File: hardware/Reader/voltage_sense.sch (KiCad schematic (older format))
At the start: 5 parts

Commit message: Fixed bugs on the reader schematic. Exported Schematic Electrical report
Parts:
- C_VS_1: Manufacturer (none) -> Yageo; Part Name (none) -> CC0603JRX7R8BB104; Vendor (none) -> DigiKey Canada; digikeypn (none) -> 311-1777-1-ND
- D_VS_1, D_VS_2: Manufacturer (none) -> STMicroelectronics; Part Name (none) -> BAT46; Vendor (none) -> DigiKey Canada; digikeypn (none) -> 497-3768-1-ND
- R_VS_1: Manufacturer (none) -> Panasonic Electronic Components; Vendor (none) -> DigiKey Canada; digikeypn (none) -> P123106CT-ND
- R_VS_2: Manufacturer (none) -> Panasonic Electronic Components; Vendor (none) -> DigiKey Canada; digikeypn (none) -> P122414CT-ND
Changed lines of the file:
@@
 $Descr USLetter 11000 8500
 encoding utf-8
-Sheet 16 19
+Sheet 17 19
 Title "CANnect Reader | Voltage Sense"
 Date "2020-10-25"
@@
 Comment4 "Component Identifier: VS"
 $EndDescr
+Wire Notes Line
+	1750 1350 1750 4150
+Wire Notes Line
+	1750 4150 4650 4150
+Wire Notes Line
+	4650 4150 4650 1350
+Wire Notes Line
+	4650 1350 1750 1350
+Text Notes 2050 1500 2    50   ~ 0
+Typical
+Wire Wire Line
+	2850 2050 2850 1750
 $Comp
-L Device:R_Small R_VS_2
-U 1 1 5FD5DF8C
-P 2850 2800
-F 0 "R_VS_2" H 2909 2846 50  0000 L CNN
-F 1 "10k 1%" H 2909 2755 50  0000 L CNN
-F 2 "footprints:RESC3216X70N" H 2850 2800 50  0001 C CNN
-F 3 "https://industrial.panasonic.com/cdbs/www-data/pdf/RDA0000/AOA0000C304.pdf" H 2850 2800 50  0001 C CNN
-F 4 "ERJ-1GNF1002C" H 2850 2800 50  0001 C CNN "Part Name"
-	1    2850 2800
+L Device:R_Small R_VS_1
+U 1 1 6007733F
+P 2850 2150
+F 0 "R_VS_1" H 2909 2196 50  0000 L CNN
+F 1 "62k 1%" H 2909 2105 50  0000 L CNN
+F 2 "footprints:RESC3216X70N" H 2850 2150 50  0001 C CNN
+F 3 "https://industrial.panasonic.com/cdbs/www-data/pdf/RDA0000/AOA0000C304.pdf" H 2850 2150 50  0001 C CNN
+F 4 "ERJ-1GNF6202C" H 2850 2150 50  0001 C CNN "Part Name"
+F 5 "Panasonic Electronic Components" H 2850 2150 50  0001 C CNN "Manufacturer"
+F 6 "DigiKey Canada" H 2850 2150 50  0001 C CNN "Vendor"
+F 7 "P123106CT-ND" H 2850 2150 50  0001 C CNN "digikeypn"
+	1    2850 2150
+	1    0    0    -1
+$EndComp
+Wire Wire Line
+	3400 2000 3400 1750
+$Comp
+L power:+3.3V #PWR0123
+U 1 1 5FD61353
+P 3400 1750
+F 0 "#PWR0123" H 3400 1600 50  0001 C CNN
+F 1 "+3.3V" H 3415 1923 50  0000 C CNN
+F 2 "" H 3400 1750 50  0001 C CNN
+F 3 "" H 3400 1750 50  0001 C CNN
+	1    3400 1750
+	1    0    0    -1
+$EndComp
+Wire Wire Line
+	3400 3650 3400 3000
+$Comp
+L power:GND #PWR0122
+U 1 1 5FD60B0C
+P 3400 3650
+F 0 "#PWR0122" H 3400 3400 50  0001 C CNN
+F 1 "GND" H 3405 3477 50  0000 C CNN
+F 2 "" H 3400 3650 50  0001 C CNN
+F 3 "" H 3400 3650 50  0001 C CNN
+	1    3400 3650
+	1    0    0    -1
+$EndComp
+Wire Wire Line
+	3400 2500 3400 2700
+Wire Wire Line
+	3400 2500 3950 2500
+Wire Wire Line
+	2850 2500 3400 2500
+Connection ~ 3400 2500
+Wire Wire Line
+	3400 2500 3400 2300
+$Comp
+L Diode:BAT46 D_VS_1
+U 1 1 5FD600B9
+P 3400 2150
+F 0 "D_VS_1" V 3354 2230 50  0000 L CNN
+F 1 "BAT46" V 3445 2230 50  0000 L CNN
+F 2 "Diode_THT:D_DO-35_SOD27_P7.62mm_Horizontal" H 3400 1975 50  0001 C CNN
+F 3 "http://www.vishay.com/docs/85662/bat46.pdf" H 3400 2150 50  0001 C CNN
+F 4 "BAT46" H 3400 2150 50  0001 C CNN "Part Name"
+F 5 "STMicroelectronics" H 3400 2150 50  0001 C CNN "Manufacturer"
+F 6 "DigiKey Canada" H 3400 2150 50  0001 C CNN "Vendor"
+F 7 "497-3768-1-ND" H 3400 2150 50  0001 C CNN "digikeypn"
+	1    3400 2150
+	0    1    1    0
+$EndComp
+$Comp
+L Diode:BAT46 D_VS_2
+U 1 1 5FD5FBA4
+P 3400 2850
+F 0 "D_VS_2" V 3354 2930 50  0000 L CNN
+F 1 "BAT46" V 3445 2930 50  0000 L CNN
+F 2 "Diode_THT:D_DO-35_SOD27_P7.62mm_Horizontal" H 3400 2675 50  0001 C CNN
+F 3 "http://www.vishay.com/docs/85662/bat46.pdf" H 3400 2850 50  0001 C CNN
+F 4 "BAT46" H 3400 2850 50  0001 C CNN "Part Name"
+F 5 "STMicroelectronics" H 3400 2850 50  0001 C CNN "Manufacturer"
+F 6 "DigiKey Canada" H 3400 2850 50  0001 C CNN "Vendor"
+F 7 "497-3768-1-ND" H 3400 2850 50  0001 C CNN "digikeypn"
+	1    3400 2850
+	0    1    1    0
+$EndComp
+Text HLabel 3950 2500 2    50   Output ~ 0
+Analog_Voltage
+$Comp
+L power:GND #PWR0112
+U 1 1 5FD5EC70
+P 2850 3650
+F 0 "#PWR0112" H 2850 3400 50  0001 C CNN
+F 1 "GND" H 2855 3477 50  0000 C CNN
+F 2 "" H 2850 3650 50  0001 C CNN
+F 3 "" H 2850 3650 50  0001 C CNN
+	1    2850 3650
+	1    0    0    -1
+$EndComp
+Wire Wire Line
+	2850 3300 2850 3650
+Wire Wire Line
+	2850 3300 2850 2900
+Connection ~ 2850 3300
+Wire Wire Line
+	2250 3300 2850 3300
+Wire Wire Line
+	2250 2950 2250 3300
+Wire Wire Line
+	2850 2500 2850 2250
+Wire Wire Line
+	2850 2500 2850 2700
+Connection ~ 2850 2500
+Wire Wire Line
+	2250 2500 2850 2500
+Wire Wire Line
+	2250 2650 2250 2500
+$Comp
+L Device:C C_VS_1
+U 1 1 5FD5E63B
+P 2250 2800
+F 0 "C_VS_1" H 2365 2846 50  0000 L CNN
+F 1 "0.1uF" H 2365 2755 50  0000 L CNN
+F 2 "footprints:CAPC1608X90" H 2288 2650 50  0001 C CNN
+F 3 "https://www.yageo.com/upload/media/product/productsearch/datasheet/mlcc/UPY-GPHC_X7R_6.3V-to-50V_18.pdf" H 2250 2800 50  0001 C CNN
+F 4 "CC0603JRX7R8BB104" H 2250 2800 50  0001 C CNN "Part Name"
+F 5 "Yageo" H 2250 2800 50  0001 C CNN "Manufacturer"
+F 6 "DigiKey Canada" H 2250 2800 50  0001 C CNN "Vendor"
+F 7 "311-1777-1-ND" H 2250 2800 50  0001 C CNN "digikeypn"
+	1    2250 2800
 	1    0    0    -1
 $EndComp
@@
 $EndComp
 $Comp
-L Device:C C_VS_1
-U 1 1 5FD5E63B
-P 2250 2800
-F 0 "C_VS_1" H 2365 2846 50  0000 L CNN
-F 1 "0.1uF" H 2365 2755 50  0000 L CNN
-F 2 "footprints:CAPC1608X90" H 2288 2650 50  0001 C CNN
-F 3 "https://www.yageo.com/upload/media/product/productsearch/datasheet/mlcc/UPY-GPHC_X7R_6.3V-to-50V_18.pdf" H 2250 2800 50  0001 C CNN
-	1    2250 2800
+L Device:R_Small R_VS_2
+U 1 1 5FD5DF8C
+P 2850 2800
+F 0 "R_VS_2" H 2909 2846 50  0000 L CNN
+F 1 "10k 1%" H 2909 2755 50  0000 L CNN
+F 2 "footprints:RESC3216X70N" H 2850 2800 50  0001 C CNN
+F 3 "https://industrial.panasonic.com/cdbs/www-data/pdf/RDA0000/AOA0000C304.pdf" H 2850 2800 50  0001 C CNN
+F 4 "ERJ-1GNF1002C" H 2850 2800 50  0001 C CNN "Part Name"
+F 5 "Panasonic Electronic Components" H 2850 2800 50  0001 C CNN "Manufacturer"
+F 6 "DigiKey Canada" H 2850 2800 50  0001 C CNN "Vendor"
+F 7 "P122414CT-ND" H 2850 2800 50  0001 C CNN "digikeypn"
+	1    2850 2800
 	1    0    0    -1
 $EndComp
-Wire Wire Line
-	2250 2650 2250 2500
-Wire Wire Line
-	2250 2500 2850 2500
-Connection ~ 2850 2500
-Wire Wire Line
-	2850 2500 2850 2700
-Wire Wire Line
-	2250 2950 2250 3300
-Wire Wire Line
-	2250 3300 2850 3300
-Wire Wire Line
-	2850 3300 2850 2900
-$Comp
-L power:GND #PWR0112
-U 1 1 5FD5EC70
-P 2850 3650
-F 0 "#PWR0112" H 2850 3400 50  0001 C CNN
-F 1 "GND" H 2855 3477 50  0000 C CNN
-F 2 "" H 2850 3650 50  0001 C CNN
-F 3 "" H 2850 3650 50  0001 C CNN
-	1    2850 3650
-	1    0    0    -1
-$EndComp
-Wire Wire Line
-	2850 3300 2850 3650
-Connection ~ 2850 3300
-Text HLabel 3950 2500 2    50   Output ~ 0
-Analog_Voltage
-$Comp
-L Diode:BAT46 D_VS_2
-U 1 1 5FD5FBA4
-P 3400 2850
-F 0 "D_VS_2" V 3354 2930 50  0000 L CNN
-F 1 "BAT46" V 3445 2930 50  0000 L CNN
-F 2 "Diode_THT:D_DO-35_SOD27_P7.62mm_Horizontal" H 3400 2675 50  0001 C CNN
-F 3 "http://www.vishay.com/docs/85662/bat46.pdf" H 3400 2850 50  0001 C CNN
-	1    3400 2850
-	0    1    1    0
-$EndComp
-$Comp
-L Diode:BAT46 D_VS_1
-U 1 1 5FD600B9
-P 3400 2150
-F 0 "D_VS_1" V 3354 2230 50  0000 L CNN
-F 1 "BAT46" V 3445 2230 50  0000 L CNN
-F 2 "Diode_THT:D_DO-35_SOD27_P7.62mm_Horizontal" H 3400 1975 50  0001 C CNN
-F 3 "http://www.vishay.com/docs/85662/bat46.pdf" H 3400 2150 50  0001 C CNN
-	1    3400 2150
-	0    1    1    0
-$EndComp
-Wire Wire Line
-	3400 2500 3400 2300
-Connection ~ 3400 2500
-Wire Wire Line
-	3400 2500 3400 2700
-$Comp
-L power:GND #PWR0122
-U 1 1 5FD60B0C
-P 3400 3650
-F 0 "#PWR0122" H 3400 3400 50  0001 C CNN
-F 1 "GND" H 3405 3477 50  0000 C CNN
-F 2 "" H 3400 3650 50  0001 C CNN
-F 3 "" H 3400 3650 50  0001 C CNN
-	1    3400 3650
-	1    0    0    -1
-$EndComp
-Wire Wire Line
-	3400 3650 3400 3000
-$Comp
-L power:+3.3V #PWR0123
-U 1 1 5FD61353
-P 3400 1750
-F 0 "#PWR0123" H 3400 1600 50  0001 C CNN
-F 1 "+3.3V" H 3415 1923 50  0000 C CNN
-F 2 "" H 3400 1750 50  0001 C CNN
-F 3 "" H 3400 1750 50  0001 C CNN
-	1    3400 1750
-	1    0    0    -1
-$EndComp
-Wire Wire Line
-	3400 2000 3400 1750
-Wire Wire Line
-	2850 2500 3400 2500
-Wire Wire Line
-	3400 2500 3950 2500
-Wire Notes Line
-	1750 1350 1750 4150
-Wire Notes Line
-	1750 4150 4650 4150
-Wire Notes Line
-	4650 4150 4650 1350
-Wire Notes Line
-	4650 1350 1750 1350
-Text Notes 2050 1500 2    50   ~ 0
-Typical
-$Comp
-L Device:R_Small R_VS_1
-U 1 1 6007733F
-P 2850 2150
-F 0 "R_VS_1" H 2909 2196 50  0000 L CNN
-F 1 "62k 1%" H 2909 2105 50  0000 L CNN
-F 2 "footprints:RESC3216X70N" H 2850 2150 50  0001 C CNN
-F 3 "https://industrial.panasonic.com/cdbs/www-data/pdf/RDA0000/AOA0000C304.pdf" H 2850 2150 50  0001 C CNN
-F 4 "ERJ-1GNF6202C" H 2850 2150 50  0001 C CNN "Part Name"
-	1    2850 2150
-	1    0    0    -1
-$EndComp
-Wire Wire Line
-	2850 2050 2850 1750
-Wire Wire Line
-	2850 2500 2850 2250
 $EndSCHEMATC

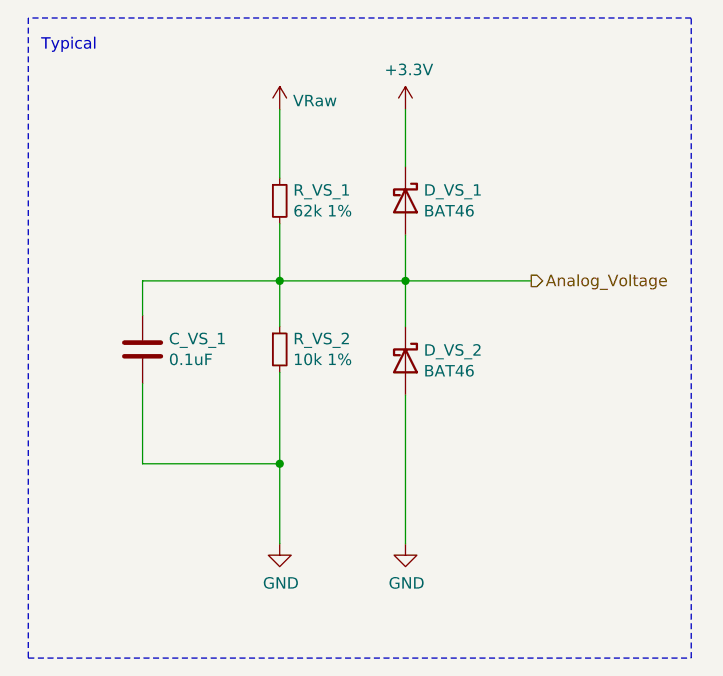
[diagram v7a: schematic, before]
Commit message: Fixed numerous bugs in design for Reader Schematic and PCB
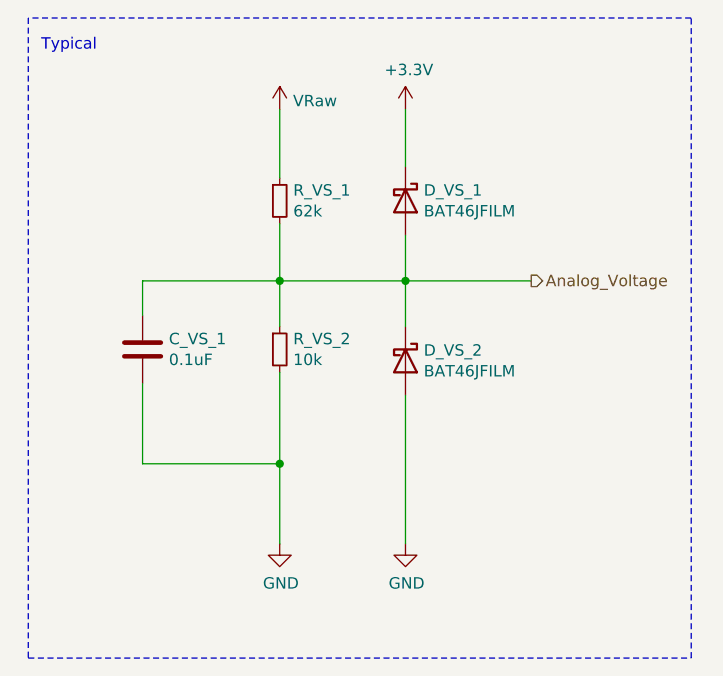
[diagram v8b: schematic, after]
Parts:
- D_VS_1, D_VS_2: value BAT46 -> BAT46JFILM; footprint Diode_THT:D_DO-35_SOD27_P7.62mm_Horizontal -> footprints:BAT46JFILM; Part Name BAT46 -> BAT46JFILM; digikeypn 497-3768-1-ND -> 497-6653-1-ND
- R_VS_1: value 62k 1% -> 62k; footprint footprints:RESC3216X70N -> footprints:RESC2012X60N; Manufacturer Panasonic Electronic Components -> Yageo; Part Name ERJ-1GNF6202C -> RT0805FRE0762KL; digikeypn P123106CT-ND -> 13-RT0805FRE0762KLCT-ND
- R_VS_2: value 10k 1% -> 10k; footprint footprints:RESC3216X70N -> footprints:RESC1608X55N; Manufacturer Panasonic Electronic Components -> Yageo; Part Name ERJ-1GNF1002C -> RT0603FRE0710KL; digikeypn P122414CT-ND -> YAG2321CT-ND
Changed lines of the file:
@@
 P 2850 2150
 F 0 "R_VS_1" H 2909 2196 50  0000 L CNN
-F 1 "62k 1%" H 2909 2105 50  0000 L CNN
-F 2 "footprints:RESC3216X70N" H 2850 2150 50  0001 C CNN
-F 3 "https://industrial.panasonic.com/cdbs/www-data/pdf/RDA0000/AOA0000C304.pdf" H 2850 2150 50  0001 C CNN
-F 4 "ERJ-1GNF6202C" H 2850 2150 50  0001 C CNN "Part Name"
-F 5 "Panasonic Electronic Components" H 2850 2150 50  0001 C CNN "Manufacturer"
+F 1 "62k" H 2909 2105 50  0000 L CNN
+F 2 "footprints:RESC2012X60N" H 2850 2150 50  0001 C CNN
+F 3 "https://www.yageo.com/upload/media/product/productsearch/datasheet/rchip/PYu-RT_1-to-0.01_RoHS_L_12.pdf" H 2850 2150 50  0001 C CNN
+F 4 "RT0805FRE0762KL" H 2850 2150 50  0001 C CNN "Part Name"
+F 5 "Yageo" H 2850 2150 50  0001 C CNN "Manufacturer"
 F 6 "DigiKey Canada" H 2850 2150 50  0001 C CNN "Vendor"
-F 7 "P123106CT-ND" H 2850 2150 50  0001 C CNN "digikeypn"
+F 7 "13-RT0805FRE0762KLCT-ND" H 2850 2150 50  0001 C CNN "digikeypn"
 	1    2850 2150
 	1    0    0    -1
@@
 P 3400 2150
 F 0 "D_VS_1" V 3354 2230 50  0000 L CNN
-F 1 "BAT46" V 3445 2230 50  0000 L CNN
-F 2 "Diode_THT:D_DO-35_SOD27_P7.62mm_Horizontal" H 3400 1975 50  0001 C CNN
-F 3 "http://www.vishay.com/docs/85662/bat46.pdf" H 3400 2150 50  0001 C CNN
-F 4 "BAT46" H 3400 2150 50  0001 C CNN "Part Name"
+F 1 "BAT46JFILM" V 3445 2230 50  0000 L CNN
+F 2 "footprints:BAT46JFILM" H 3400 1975 50  0001 C CNN
+F 3 "https://www.st.com/content/ccc/resource/technical/document/datasheet/c6/32/d4/4a/28/d3/4b/11/CD00004930.pdf/files/CD00004930.pdf/jcr:content/translations/en.CD00004930.pdf" H 3400 2150 50  0001 C CNN
+F 4 "BAT46JFILM" H 3400 2150 50  0001 C CNN "Part Name"
 F 5 "STMicroelectronics" H 3400 2150 50  0001 C CNN "Manufacturer"
 F 6 "DigiKey Canada" H 3400 2150 50  0001 C CNN "Vendor"
-F 7 "497-3768-1-ND" H 3400 2150 50  0001 C CNN "digikeypn"
+F 7 "497-6653-1-ND" H 3400 2150 50  0001 C CNN "digikeypn"
 	1    3400 2150
 	0    1    1    0
@@
 P 3400 2850
 F 0 "D_VS_2" V 3354 2930 50  0000 L CNN
-F 1 "BAT46" V 3445 2930 50  0000 L CNN
-F 2 "Diode_THT:D_DO-35_SOD27_P7.62mm_Horizontal" H 3400 2675 50  0001 C CNN
-F 3 "http://www.vishay.com/docs/85662/bat46.pdf" H 3400 2850 50  0001 C CNN
-F 4 "BAT46" H 3400 2850 50  0001 C CNN "Part Name"
+F 1 "BAT46JFILM" V 3445 2930 50  0000 L CNN
+F 2 "footprints:BAT46JFILM" H 3400 2675 50  0001 C CNN
+F 3 "https://www.st.com/content/ccc/resource/technical/document/datasheet/c6/32/d4/4a/28/d3/4b/11/CD00004930.pdf/files/CD00004930.pdf/jcr:content/translations/en.CD00004930.pdf" H 3400 2850 50  0001 C CNN
+F 4 "BAT46JFILM" H 3400 2850 50  0001 C CNN "Part Name"
 F 5 "STMicroelectronics" H 3400 2850 50  0001 C CNN "Manufacturer"
 F 6 "DigiKey Canada" H 3400 2850 50  0001 C CNN "Vendor"
-F 7 "497-3768-1-ND" H 3400 2850 50  0001 C CNN "digikeypn"
+F 7 "497-6653-1-ND" H 3400 2850 50  0001 C CNN "digikeypn"
 	1    3400 2850
 	0    1    1    0
@@
 P 2850 2800
 F 0 "R_VS_2" H 2909 2846 50  0000 L CNN
-F 1 "10k 1%" H 2909 2755 50  0000 L CNN
-F 2 "footprints:RESC3216X70N" H 2850 2800 50  0001 C CNN
-F 3 "https://industrial.panasonic.com/cdbs/www-data/pdf/RDA0000/AOA0000C304.pdf" H 2850 2800 50  0001 C CNN
-F 4 "ERJ-1GNF1002C" H 2850 2800 50  0001 C CNN "Part Name"
-F 5 "Panasonic Electronic Components" H 2850 2800 50  0001 C CNN "Manufacturer"
+F 1 "10k" H 2909 2755 50  0000 L CNN
+F 2 "footprints:RESC1608X55N" H 2850 2800 50  0001 C CNN
+F 3 "https://www.yageo.com/upload/media/product/productsearch/datasheet/rchip/PYu-RT_1-to-0.01_RoHS_L_12.pdf" H 2850 2800 50  0001 C CNN
+F 4 "RT0603FRE0710KL" H 2850 2800 50  0001 C CNN "Part Name"
+F 5 "Yageo" H 2850 2800 50  0001 C CNN "Manufacturer"
 F 6 "DigiKey Canada" H 2850 2800 50  0001 C CNN "Vendor"
-F 7 "P122414CT-ND" H 2850 2800 50  0001 C CNN "digikeypn"
+F 7 "YAG2321CT-ND" H 2850 2800 50  0001 C CNN "digikeypn"
 	1    2850 2800
 	1    0    0    -1
